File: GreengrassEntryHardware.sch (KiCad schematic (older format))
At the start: 29 parts, among them J1 USB_B_Micro, J2 GPIOBreakout, J3 Raspberry_Pi_2_3, J4 AutomaticSlidingDoor, J5 MFRC-522, U1 CH340G, Y1 12MHZ

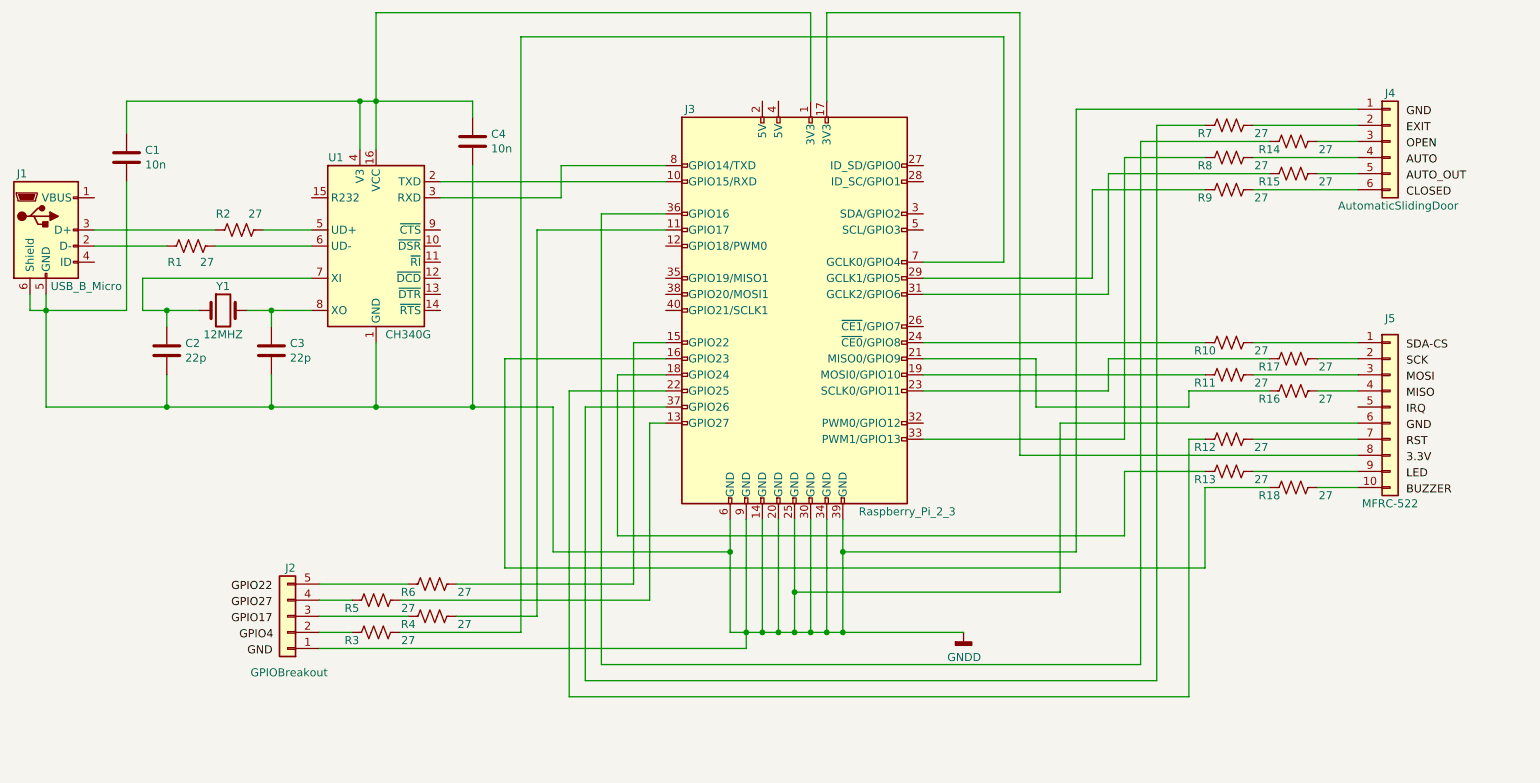
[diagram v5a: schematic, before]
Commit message: Added a status led
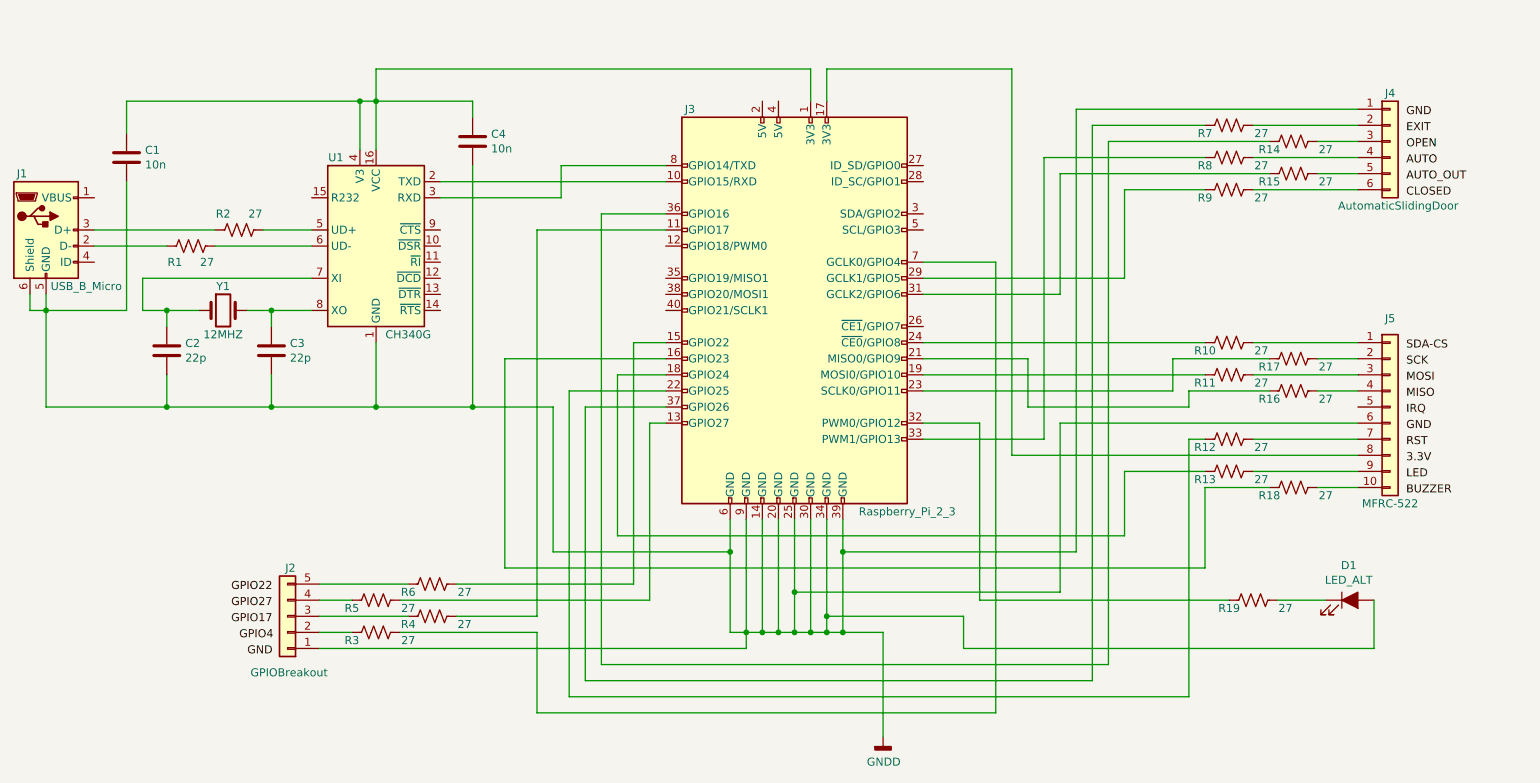
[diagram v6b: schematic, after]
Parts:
- added D1: LED_ALT, LED_SMD:LED_0805_2012Metric_Pad1.15x1.40mm_HandSolder, symbol Device:LED_ALT
- added R19: 27, Resistor_SMD:R_0805_2012Metric_Pad1.15x1.40mm_HandSolder, symbol Device:R_US
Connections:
- net GNDD: now also D1.2 (A)
- net at J3.32 (PWM0/GPIO12): now also R19.2
- new net: D1.1 (K), R19.1
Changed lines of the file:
@@
 $EndComp
-Wire Wire Line
-	6100 2000 6100 2550
 Wire Wire Line
 	5100 4350 4500 4350
@@
 	3700 3150 4450 3150
 Wire Wire Line
-	6000 2000 6000 2550
-Wire Wire Line
-	6100 2000 7300 2000
-Wire Wire Line
 	7550 5600 5900 5600
 Wire Wire Line
 	5900 5600 5900 5150
 Wire Wire Line
-	8150 6150 4600 6150
-Wire Wire Line
 	4600 6150 4600 4450
 Wire Wire Line
 	4600 4450 5100 4450
-Wire Wire Line
-	7950 4650 6700 4650
-Wire Wire Line
-	7850 3750 6700 3750
-Wire Wire Line
-	7750 3650 6700 3650
-Wire Wire Line
-	7850 4150 7850 4350
-Wire Wire Line
-	6700 4350 7850 4350
-Wire Wire Line
-	7400 4450 7400 4150
-Wire Wire Line
-	7400 4150 6700 4150
 Wire Wire Line
 	3300 4450 3900 4450
@@
 Wire Wire Line
 	4800 4250 5100 4250
-Wire Wire Line
-	8050 6050 4700 6050
 Wire Wire Line
 	4700 3250 5100 3250
@@
 $EndComp
 Wire Wire Line
-	7400 4450 8350 4450
-Wire Wire Line
 	8350 4450 8350 4350
 Wire Wire Line
@@
 	0    1    1    0
 $EndComp
-Wire Wire Line
-	7300 4750 7300 2000
 $Comp
 L Device:R_US R7
@@
 Wire Wire Line
 	9400 4650 8750 4650
-Wire Wire Line
-	9400 4750 7300 4750
 Wire Wire Line
 	4700 3250 4700 6050
@@
 Wire Wire Line
 	4300 3350 5100 3350
-Wire Wire Line
-	7200 2150 7200 3550
-Wire Wire Line
-	7200 3550 6700 3550
-Wire Wire Line
-	4200 2150 7200 2150
 $Comp
 L Device:R_US R3
@@
 	4800 5250 4800 4250
 Wire Wire Line
-	6000 2000 3300 2000
-Wire Wire Line
-	3300 2000 3300 2550
-Wire Wire Line
 	3700 3050 5100 3050
 Wire Wire Line
@@
 L power:GNDD #PWR0101
 U 1 1 5D3B21CF
-P 6950 5850
-F 0 "#PWR0101" H 6950 5600 50  0001 C CNN
-F 1 "GNDD" H 6954 5695 50  0000 C CNN
-F 2 "" H 6950 5850 50  0001 C CNN
-F 3 "" H 6950 5850 50  0001 C CNN
-	1    6950 5850
+P 6450 6500
+F 0 "#PWR0101" H 6450 6250 50  0001 C CNN
+F 1 "GNDD" H 6454 6345 50  0000 C CNN
+F 2 "" H 6450 6500 50  0001 C CNN
+F 3 "" H 6450 6500 50  0001 C CNN
+	1    6450 6500
 	1    0    0    -1
 $EndComp
 Wire Wire Line
-	6950 5850 6200 5850
-Wire Wire Line
 	6200 5850 6100 5850
-Wire Wire Line
-	6100 5850 6100 5150
 Connection ~ 6200 5850
 Wire Wire Line
@@
 Wire Wire Line
 	2950 5550 3500 5550
-Wire Wire Line
-	3450 5850 4200 5850
-Wire Wire Line
-	4200 2150 4200 5850
 Wire Wire Line
 	3800 5750 4300 5750
@@
 	9150 4150 9400 4150
 Wire Wire Line
-	8850 4150 7850 4150
+	8850 4150 8250 4150
 Wire Wire Line
 	9150 4950 9400 4950
@@
 	7650 2600 7650 5350
 Wire Wire Line
-	8150 6150 8150 2700
-Wire Wire Line
-	8150 2700 8450 2700
-Wire Wire Line
-	8850 2800 8050 2800
-Wire Wire Line
-	8050 2800 8050 6050
-Wire Wire Line
-	8450 2900 7950 2900
-Wire Wire Line
-	7950 2900 7950 4650
-Wire Wire Line
-	8850 3000 7850 3000
-Wire Wire Line
-	7850 3000 7850 3750
-Wire Wire Line
-	8450 3100 7750 3100
-Wire Wire Line
-	7750 3100 7750 3650
+	6700 3750 7550 3750
+Wire Wire Line
+	6700 3650 7950 3650
+Wire Wire Line
+	7750 2700 7750 6150
+Wire Wire Line
+	7750 6150 4600 6150
+Wire Wire Line
+	7750 2700 8450 2700
+Wire Wire Line
+	8250 4350 8250 4150
+Wire Wire Line
+	6700 4350 8250 4350
+Wire Wire Line
+	7850 2800 7850 6050
+Wire Wire Line
+	7850 6050 4700 6050
+Wire Wire Line
+	7850 2800 8850 2800
+Wire Wire Line
+	7450 2900 7450 4650
+Wire Wire Line
+	7450 4650 6700 4650
+Wire Wire Line
+	7350 4150 7350 4450
+Wire Wire Line
+	7350 4150 6700 4150
+Wire Wire Line
+	7350 4450 8350 4450
+Wire Wire Line
+	7150 3550 6700 3550
+Wire Wire Line
+	7250 4750 9400 4750
+Wire Wire Line
+	7450 2900 8450 2900
+Wire Wire Line
+	7550 3000 7550 3750
+Wire Wire Line
+	7550 3000 8850 3000
+Wire Wire Line
+	7950 3650 7950 3100
+Wire Wire Line
+	7950 3100 8450 3100
+Wire Wire Line
+	7150 6350 7150 3550
+Wire Wire Line
+	6450 6500 6450 5850
+Wire Wire Line
+	6200 5850 6450 5850
+Wire Wire Line
+	3300 2350 6000 2350
+Wire Wire Line
+	3300 2350 3300 2550
+Wire Wire Line
+	6000 2350 6000 2550
+Wire Wire Line
+	6100 2350 7250 2350
+Wire Wire Line
+	6100 2350 6100 2550
+Wire Wire Line
+	7250 2350 7250 4750
+Wire Wire Line
+	4300 5850 4300 6350
+Wire Wire Line
+	4300 6350 7150 6350
+Wire Wire Line
+	3450 5850 4300 5850
+$Comp
+L Device:LED_ALT D1
+U 1 1 5DAC367B
+P 9350 5650
+F 0 "D1" H 9343 5866 50  0000 C CNN
+F 1 "LED_ALT" H 9343 5775 50  0000 C CNN
+F 2 "LED_SMD:LED_0805_2012Metric_Pad1.15x1.40mm_HandSolder" H 9350 5650 50  0001 C CNN
+F 3 "~" H 9350 5650 50  0001 C CNN
+	1    9350 5650
+	1    0    0    -1
+$EndComp
+$Comp
+L Device:R_US R19
+U 1 1 5DAC3A84
+P 8750 5650
+F 0 "R19" V 8800 5500 50  0000 C CNN
+F 1 "27" V 8800 5850 50  0000 C CNN
+F 2 "Resistor_SMD:R_0805_2012Metric_Pad1.15x1.40mm_HandSolder" V 8790 5640 50  0001 C CNN
+F 3 "~" H 8750 5650 50  0001 C CNN
+	1    8750 5650
+	0    1    1    0
+$EndComp
+Wire Wire Line
+	8900 5650 9200 5650
+Wire Wire Line
+	9500 5650 9500 5950
+Wire Wire Line
+	8600 5650 7050 5650
+Wire Wire Line
+	7050 5650 7050 4550
+Wire Wire Line
+	7050 4550 6700 4550
+Wire Wire Line
+	6100 5150 6100 5750
+Wire Wire Line
+	6950 5950 6950 5750
+Wire Wire Line
+	6950 5750 6100 5750
+Wire Wire Line
+	6950 5950 9500 5950
+Connection ~ 6100 5750
+Wire Wire Line
+	6100 5750 6100 5850
 $EndSCHEMATC

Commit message: Added molex connector for mfrc and added net labels
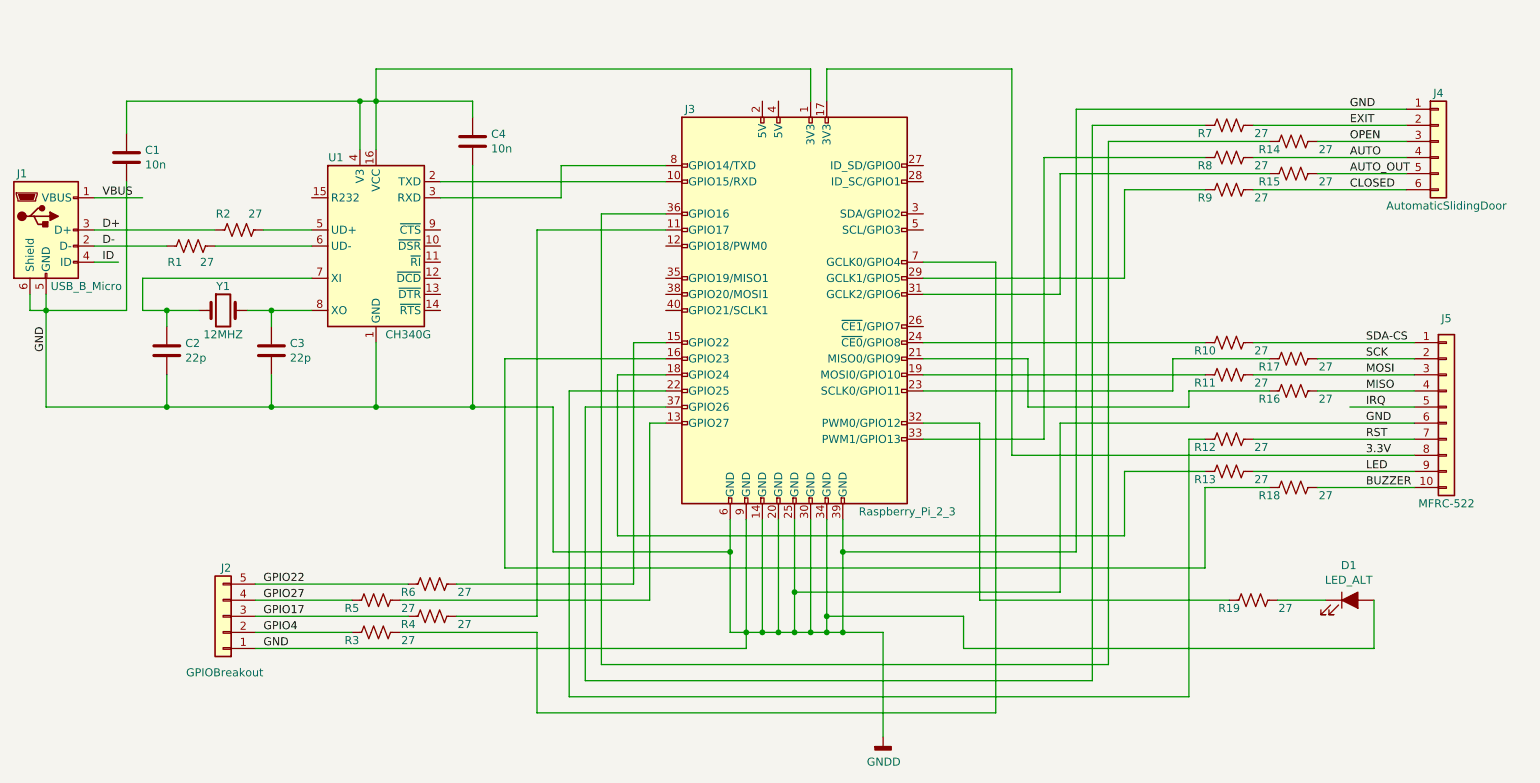
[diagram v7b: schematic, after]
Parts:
- J5: footprint Connector_PinHeader_2.54mm:PinHeader_2x05_P2.54mm_Horizontal -> GreengrassEntryHardware:Molex_Micro-Fit_3.0_43045-1000_2x05_P3.00mm_Horizontal
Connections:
- net 3.3V: now also J3.17 (3V3), J5.8 (Pin_8)
- net AUTO: now also J4.4 (Pin_4), R8.1
- net AUTO_OUT: now also J4.5 (Pin_5), R15.1
- net BUZZER: now also J5.10 (Pin_10), R18.1
- net CLOSED: now also J4.6 (Pin_6), R9.1
- net EXIT: now also J4.2 (Pin_2), R7.1
- net GPIO17: now also J2.3 (Pin_3), R4.2
- net GPIO22: now also J2.5 (Pin_5), R6.2
- net GPIO27: now also J2.4 (Pin_4), R5.2
- net GPIO4: now also J2.2 (Pin_2), R3.2
- net IRQ: now also J5.5 (Pin_5)
- net LED: now also J5.9 (Pin_9), R13.1
- net MISO: now also J5.4 (Pin_4), R16.1
- net MOSI: now also J5.3 (Pin_3), R11.1
- net OPEN: now also J4.3 (Pin_3), R14.1
- net RST: now also J5.7 (Pin_7), R12.1
- net SCK: now also J5.2 (Pin_2), R17.1
- net SDA-CS: now also J5.1 (Pin_1), R10.1
- net VBUS: now reaches J1.1 (VBUS)
- net D-: now reaches J1.2 (D-), R1.2
- net D+: now reaches J1.3 (D+), R2.2
- net ID: now reaches J1.4 (ID)
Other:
- moved on the sheet: J2, J4, J5
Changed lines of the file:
@@
 	1    0    0    -1
 $EndComp
-Text Label 9700 4500 0    50   ~ 0
+Text Label 9450 4450 0    50   ~ 0
 IRQ
-Text Label 9700 4800 0    50   ~ 0
+Text Label 9450 4750 0    50   ~ 0
 3.3V
-Text Label 9700 4700 0    50   ~ 0
+Text Label 9450 4650 0    50   ~ 0
 RST
-Text Label 9700 4600 0    50   ~ 0
+Text Label 9450 4550 0    50   ~ 0
 GND
-Text Label 9700 4400 0    50   ~ 0
+Text Label 9450 4350 0    50   ~ 0
 MISO
-Text Label 9700 4300 0    50   ~ 0
+Text Label 9450 4250 0    50   ~ 0
 MOSI
-Text Label 9700 4200 0    50   ~ 0
+Text Label 9450 4150 0    50   ~ 0
 SCK
-Text Label 9700 4100 0    50   ~ 0
+Text Label 9450 4050 0    50   ~ 0
 SDA-CS
 $Comp
 L Connector_Generic:Conn_01x10 J5
 U 1 1 5D3BD9C3
-P 9600 4450
-F 0 "J5" H 9600 5000 50  0000 C CNN
-F 1 "MFRC-522" H 9600 3850 50  0000 C CNN
-F 2 "Connector_PinHeader_2.54mm:PinHeader_2x05_P2.54mm_Horizontal" H 9600 4450 50  0001 C CNN
-F 3 "~" H 9600 4450 50  0001 C CNN
-	1    9600 4450
+P 9950 4450
+F 0 "J5" H 9950 5000 50  0000 C CNN
+F 1 "MFRC-522" H 9950 3850 50  0000 C CNN
+F 2 "GreengrassEntryHardware:Molex_Micro-Fit_3.0_43045-1000_2x05_P3.00mm_Horizontal" H 9950 4450 50  0001 C CNN
+F 3 "~" H 9950 4450 50  0001 C CNN
+	1    9950 4450
 	1    0    0    -1
 $EndComp
@@
 Wire Wire Line
 	4500 4350 4500 6250
-Text Label 9700 2650 0    50   ~ 0
-GND
-Text Label 9700 3150 0    50   ~ 0
-CLOSED
-Text Label 9700 3050 0    50   ~ 0
-AUTO_OUT
-Text Label 9700 2950 0    50   ~ 0
-AUTO
-Text Label 9700 2850 0    50   ~ 0
-OPEN
-Text Label 9700 2750 0    50   ~ 0
-EXIT
 $Comp
 L Connector_Generic:Conn_01x06 J4
 U 1 1 5D3C1839
-P 9600 2800
-F 0 "J4" H 9600 3100 50  0000 C CNN
-F 1 "AutomaticSlidingDoor" H 9650 2400 50  0000 C CNN
-F 2 "GreengrassEntryHardware:Molex_SPOX_5267-06A_1x06_P2.50mm_Horizontal" H 9600 2800 50  0001 C CNN
-F 3 "~" H 9600 2800 50  0001 C CNN
-	1    9600 2800
+P 9900 2800
+F 0 "J4" H 9900 3100 50  0000 C CNN
+F 1 "AutomaticSlidingDoor" H 9950 2400 50  0000 C CNN
+F 2 "GreengrassEntryHardware:Molex_SPOX_5267-06A_1x06_P2.50mm_Horizontal" H 9900 2800 50  0001 C CNN
+F 3 "~" H 9900 2800 50  0001 C CNN
+	1    9900 2800
 	1    0    0    -1
 $EndComp
@@
 $EndComp
 Wire Wire Line
-	8750 2700 9400 2700
-Wire Wire Line
-	9150 2800 9400 2800
-Wire Wire Line
-	9150 3000 9400 3000
-Wire Wire Line
-	8750 3100 9400 3100
-Wire Wire Line
-	9400 2900 8750 2900
-Wire Wire Line
-	8750 4050 9400 4050
-Wire Wire Line
-	8750 4250 9400 4250
-Wire Wire Line
-	9150 4350 9400 4350
-Wire Wire Line
-	9400 4550 7550 4550
-Wire Wire Line
-	9400 4650 8750 4650
-Wire Wire Line
 	4700 3250 4700 6050
 $Comp
 L Connector_Generic:Conn_01x05 J2
 U 1 1 5D4DDC0B
-P 2750 5750
-F 0 "J2" H 2700 5450 50  0000 L CNN
-F 1 "GPIOBreakout" H 2500 6100 50  0000 L CNN
-F 2 "Connector_PinHeader_2.54mm:PinHeader_1x05_P2.54mm_Horizontal" H 2750 5750 50  0001 C CNN
-F 3 "~" H 2750 5750 50  0001 C CNN
-	1    2750 5750
+P 2350 5750
+F 0 "J2" H 2300 5450 50  0000 L CNN
+F 1 "GPIOBreakout" H 2100 6100 50  0000 L CNN
+F 2 "Connector_PinHeader_2.54mm:PinHeader_1x05_P2.54mm_Horizontal" H 2350 5750 50  0001 C CNN
+F 3 "~" H 2350 5750 50  0001 C CNN
+	1    2350 5750
 	-1   0    0    1
 $EndComp
-Text Label 2500 6000 0    50   ~ 0
+Text Label 2600 5950 0    50   ~ 0
 GND
-Text Label 2450 5900 0    50   ~ 0
+Text Label 2600 5850 0    50   ~ 0
 GPIO4
-Text Label 2400 5800 0    50   ~ 0
+Text Label 2600 5750 0    50   ~ 0
 GPIO17
-Text Label 2400 5700 0    50   ~ 0
+Text Label 2600 5650 0    50   ~ 0
 GPIO27
 Wire Wire Line
@@
 	0    1    1    0
 $EndComp
-Wire Wire Line
-	2950 5650 3150 5650
-Wire Wire Line
-	2950 5750 3500 5750
-Wire Wire Line
-	2950 5850 3150 5850
 Wire Wire Line
 	4800 5250 4800 4250
@@
 	4300 3350 4300 5750
 Wire Wire Line
-	2950 5550 3500 5550
-Wire Wire Line
 	3800 5750 4300 5750
-Wire Wire Line
-	2950 5950 5600 5950
 Wire Wire Line
 	3450 5650 5000 5650
@@
 	0    1    1    0
 $EndComp
-Text Label 2400 5600 0    50   ~ 0
+Text Label 2600 5550 0    50   ~ 0
 GPIO22
-Text Label 9700 4900 0    50   ~ 0
+Text Label 9450 4850 0    50   ~ 0
 LED
 $Comp
@@
 	6200 5350 6200 5850
 Wire Wire Line
-	8750 4850 9400 4850
-Wire Wire Line
 	7950 4850 8450 4850
 $Comp
@@
 $EndComp
 Wire Wire Line
-	9150 4150 9400 4150
-Wire Wire Line
 	8850 4150 8250 4150
 Wire Wire Line
-	9150 4950 9400 4950
-Wire Wire Line
 	8850 4950 8450 4950
 Wire Wire Line
@@
 Wire Wire Line
 	4100 4150 5100 4150
-Text Label 9700 5000 0    50   ~ 0
+Text Label 9450 4950 0    50   ~ 0
 BUZZER
 Wire Wire Line
-	7650 2600 9400 2600
-Wire Wire Line
 	7650 2600 7650 5350
 Wire Wire Line
@@
 Wire Wire Line
 	7150 3550 6700 3550
-Wire Wire Line
-	7250 4750 9400 4750
 Wire Wire Line
 	7450 2900 8450 2900
@@
 Wire Wire Line
 	6100 5750 6100 5850
+Text Label 9350 2700 0    50   ~ 0
+EXIT
+Text Label 9350 2800 0    50   ~ 0
+OPEN
+Text Label 9350 2900 0    50   ~ 0
+AUTO
+Text Label 9350 3100 0    50   ~ 0
+CLOSED
+Text Label 9350 3000 0    50   ~ 0
+AUTO_OUT
+Text Label 9350 2600 0    50   ~ 0
+GND
+Wire Wire Line
+	2550 5950 5600 5950
+Wire Wire Line
+	2550 5850 3150 5850
+Wire Wire Line
+	2550 5750 3500 5750
+Wire Wire Line
+	2550 5650 3150 5650
+Wire Wire Line
+	2550 5550 3500 5550
+Wire Wire Line
+	8750 4050 9750 4050
+Wire Wire Line
+	9150 4150 9750 4150
+Wire Wire Line
+	8750 4250 9750 4250
+Wire Wire Line
+	9150 4350 9750 4350
+Wire Wire Line
+	9150 4950 9750 4950
+Wire Wire Line
+	8750 4850 9750 4850
+Wire Wire Line
+	7250 4750 9750 4750
+Wire Wire Line
+	7550 4550 9750 4550
+Wire Wire Line
+	8750 4650 9750 4650
+Wire Wire Line
+	7650 2600 9700 2600
+Wire Wire Line
+	8750 2700 9700 2700
+Wire Wire Line
+	9150 2800 9700 2800
+Wire Wire Line
+	8750 2900 9700 2900
+Wire Wire Line
+	9150 3000 9700 3000
+Wire Wire Line
+	8750 3100 9700 3100
+Wire Wire Line
+	9350 4450 9750 4450
+Text Label 1250 3950 3    50   ~ 0
+GND
+Wire Wire Line
+	1550 3550 1700 3550
+Text Label 1600 3550 0    50   ~ 0
+ID
+Text Label 1600 3450 0    50   ~ 0
+D-
+Text Label 1600 3350 0    50   ~ 0
+D+
+Text Label 1600 3150 0    50   ~ 0
+VBUS
+Wire Wire Line
+	1550 3150 1850 3150
 $EndSCHEMATC

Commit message: Used wrong footprint for LED
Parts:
- D1: footprint LED_SMD:LED_0805_2012Metric_Pad1.15x1.40mm_HandSolder -> LED_SMD:LED_1206_3216Metric_Pad1.42x1.75mm_HandSolder
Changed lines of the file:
@@
 F 0 "D1" H 9343 5866 50  0000 C CNN
 F 1 "LED_ALT" H 9343 5775 50  0000 C CNN
-F 2 "LED_SMD:LED_0805_2012Metric_Pad1.15x1.40mm_HandSolder" H 9350 5650 50  0001 C CNN
+F 2 "LED_SMD:LED_1206_3216Metric_Pad1.42x1.75mm_HandSolder" H 9350 5650 50  0001 C CNN
 F 3 "~" H 9350 5650 50  0001 C CNN
 	1    9350 5650
